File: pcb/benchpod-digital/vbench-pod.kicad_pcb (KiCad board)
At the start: 4 copper layers, 98.5 x 120.2 mm, 325 parts, among them CN1 KH-FPC1.0-H2.0SMT-24P-QCHF, J1 X9555WR-2x13-6TV01, J10 Conn_02x02_Counter_Clockwise, J11 Conn_02x02_Counter_Clockwise, J4 DB2ERC-3.81-2P-BK, J5 DB2ERC-3.81-2P-BK, J6 DB2ERC-3.81-2P-BK, J7 HR911105A_C12074, SW1 TS24CA, SW2 TS24CA, U1 ICE40UP5K-SG48ITR, U10 TCAN1044VDRBRQ1, U18 SN74LVC2G66DCUR, U19 SN74LVC2G66DCUR, U2 W25Q64JVSSIQ, U20 SN74LVC2G66DCUR, U21 SN74LVC2G66DCUR, U22 SRV05-4.TCT, U23 SRV05-4.TCT, U24 SN74LVC2G66DCUR, U25 SRV05-4.TCT, U26 TPS259470ARPWR, U27 TPS259470ARPWR, U28 SRV05-4.TCT, U29 INA226AIDGSR, U30 TPS62130ARGTR, U31 AP2112K-1.2, U32 AP2112K-2.5TRG1, U33 INA226AIDGSR, U34 SRV05-4.TCT, U35 INA226AIDGSR, U5 STM32H563ZGT6, U52 AP2112K-1.8TRG1, U54 TCA9554PWR, U56 TCA9554PWR, U57 TPS259470ARPWR, U59 SY6280AAC, U6 LAN8742AI-CZ-TR, U60 SY6280AAC, U7 APS6404L-3SQR-SN, U8 TPS2116DRLR, X1 SX3M48.000B10F20TNN, Y1 6pF ±10ppm SMD2016-4P Crystal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, Y2 6pF ±10ppm SMD2016-4P Crystal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

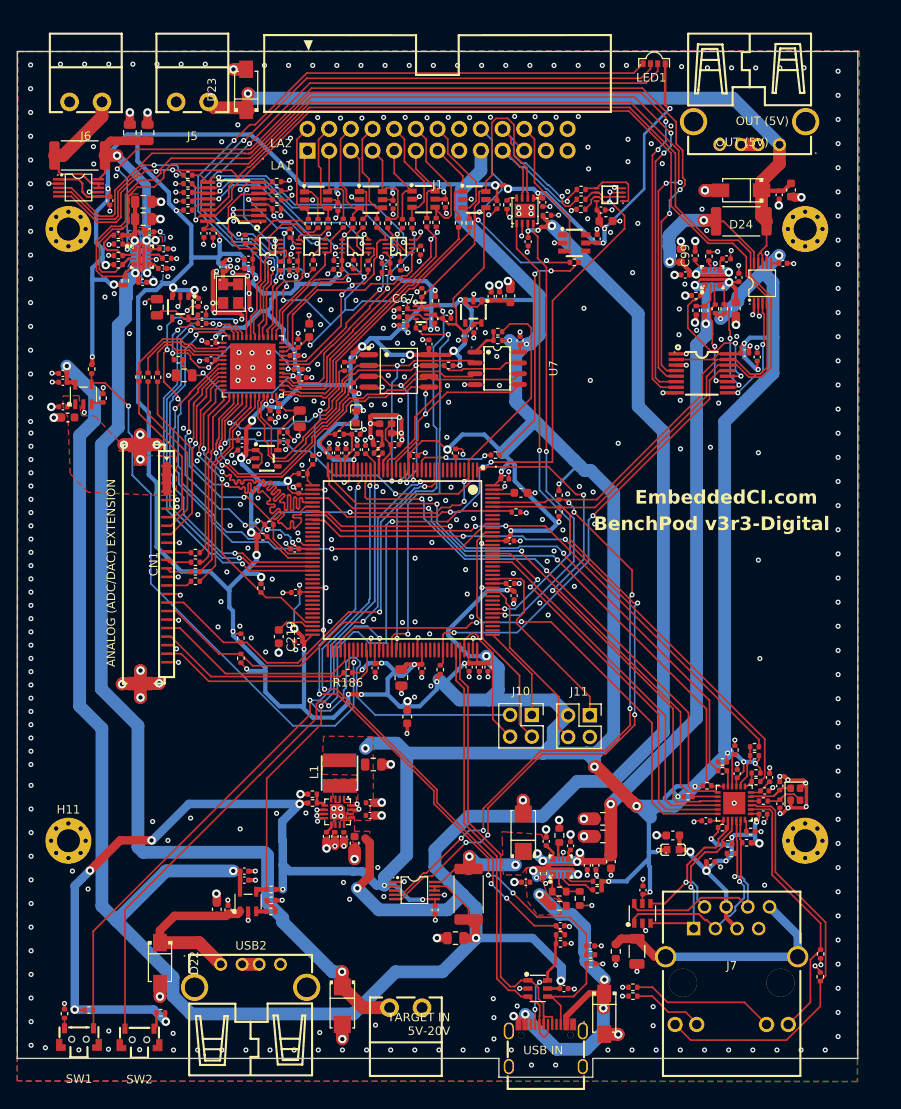
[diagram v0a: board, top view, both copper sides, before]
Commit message: digital: flush connector moves + two 2.2 mm front stop tabs
Front -y: J1 1.95, J5/J6 1.82, USB1 1.5. Back +y: J4 1.79, J7 1.72, USB2 1.55.
Stop tabs x 82.32-85.32 and 127.29-129.54, front edge to y 13.055.
Tracks not moved: reroute J1, J7, USB1, USB2 (J4/J5/J6 pads still touch old ends).

Co-Authored-By: Claude Opus 5.5 <noreply@anthropic.com>
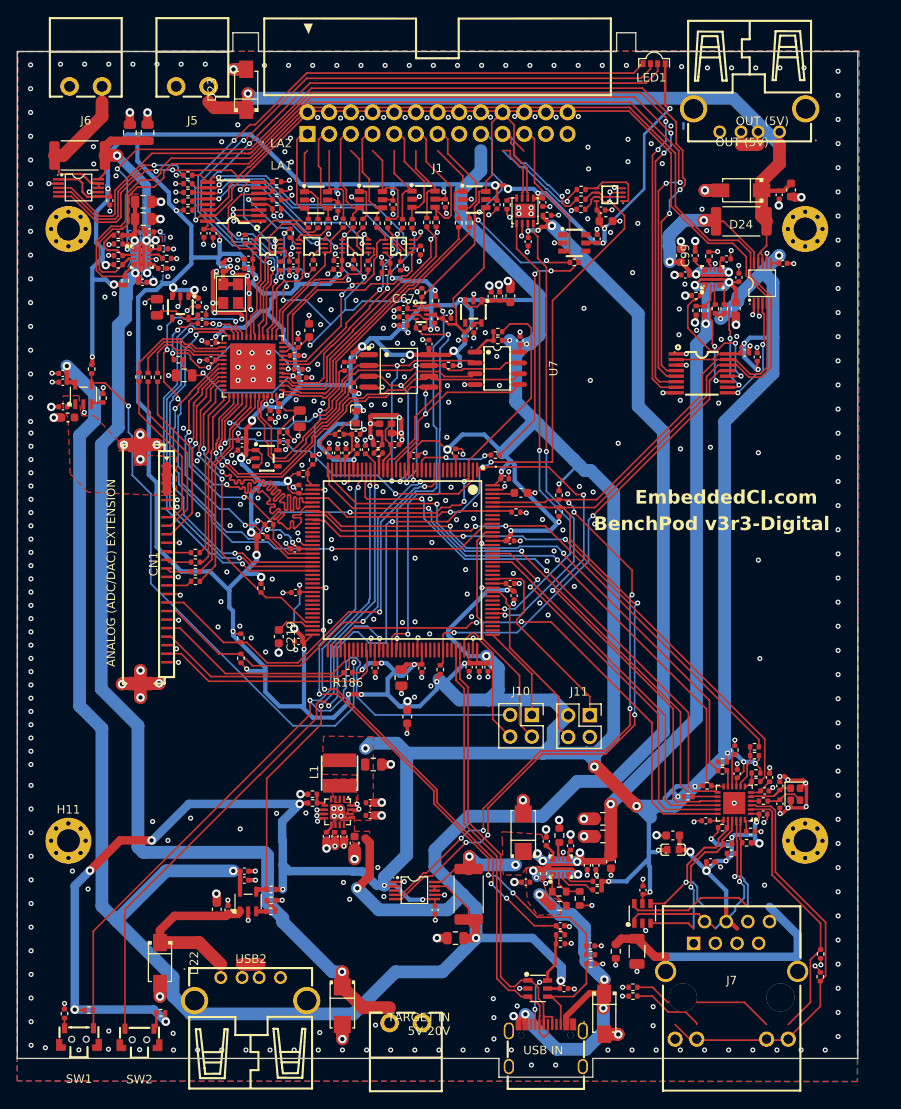
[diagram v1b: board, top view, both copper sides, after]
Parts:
- moved J1 1.95 mm to (106.3, 23.6)
- moved J5 1.82 mm to (77.6, 19.3)
- moved J6 1.82 mm to (65.1, 19.3)
- moved J4 1.79 mm to (102.6, 129.1)
- moved J7 1.72 mm to (140.8, 124.1)
- moved USB2 1.55 mm to (84.4, 125.1)
- moved USB1 1.50 mm to (142.9, 23.3)
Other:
- board size 98.5 x 120.2 mm -> 98.5 x 122.4 mm
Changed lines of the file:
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@@
 	(footprint "lcsc:RJ45-TH_HR911105A"
 		(layer "F.Cu")
-		(at 140.767569 122.389)
+		(at 140.767569 124.109)
 		(descr "RJ45-LED")
 		(property "Reference" "J7"
@@
 	(footprint "lcsc_footprints:C5259145_CONN-TH_2P-P3.81_DB2ERC-3.81-2P-BK"
 		(layer "F.Cu")
-		(at 65.080999 21.166 180)
+		(at 65.080999 19.346 180)
 		(property "Reference" "J6"
 			(at 0 -4 180)
@@
 	(footprint "lcsc_footprints:C5259145_CONN-TH_2P-P3.81_DB2ERC-3.81-2P-BK"
 		(layer "F.Cu")
-		(at 77.571 21.166 180)
+		(at 77.571 19.346 180)
 		(property "Reference" "J5"
 			(at 0 -4 0)
@@
 	(footprint "lcsc_footprints:C2682221_CONN-TH_X9555WR-2X13-6TV01"
 		(layer "F.Cu")
-		(at 106.301 25.599 180)
+		(at 106.301 23.649 180)
 		(property "Reference" "J1"
 			(at 0 -5.27 0)
@@
 	(footprint "lcsc_footprints:C5259145_CONN-TH_2P-P3.81_DB2ERC-3.81-2P-BK"
 		(layer "F.Cu")
-		(at 102.584499 127.309)
+		(at 102.584499 129.099)
 		(property "Reference" "J4"
 			(at 0 -4 0)
@@
 	(footprint "lcsc_footprints:C456018_USB-A-TH_AF-WJDG"
 		(layer "F.Cu")
-		(at 142.870998 24.823 180)
+		(at 142.870998 23.323 180)
 		(property "Reference" "USB1"
 			(at 0 -5.355 0)
@@
 	(footprint "lcsc_footprints:C456018_USB-A-TH_AF-WJDG"
 		(layer "F.Cu")
-		(at 84.397 123.576)
+		(at 84.397 125.126)
 		(property "Reference" "USB2"
 			(at 0.049 -3.533 0)
@@
 	(gr_poly
 		(pts
-			(xy 57.051 15.255) (xy 155.551 15.255) (xy 155.551 133.255) (xy 124.492 133.255) (xy 124.492 135.454999)
-			(xy 113.492 135.454999) (xy 113.492 133.255) (xy 57.051 133.255)
+			(xy 57.051 15.255) (xy 82.316 15.255) (xy 82.316 13.055) (xy 85.316 13.055) (xy 85.316 15.255) (xy 127.286 15.255)
+			(xy 127.286 13.055) (xy 129.535999 13.055) (xy 129.535999 15.255) (xy 155.551 15.255) (xy 155.551 133.255)
+			(xy 124.492 133.255) (xy 124.492 135.455) (xy 113.492 135.455) (xy 113.492 133.255) (xy 57.051 133.255)
 		)
 		(stroke
